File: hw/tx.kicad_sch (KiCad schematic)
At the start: 60 parts, among them Q301 MMBF170, Q302 MMBF170, Q303 MMBF170, Q304 MMBF170, Q305 MMBF170, Q306 MMBF170, Q307 MMBF170, Q308 MMBF170, Q309 MMBF170, Q310 MMBF170, Q311 MMBF170, Q312 MMBF170, T301 BN-43-202_DualPri_CTSec, U301 ICE40UP5K-SG48ITR, U302 CD74ACT541SM96, Y301 40MHz

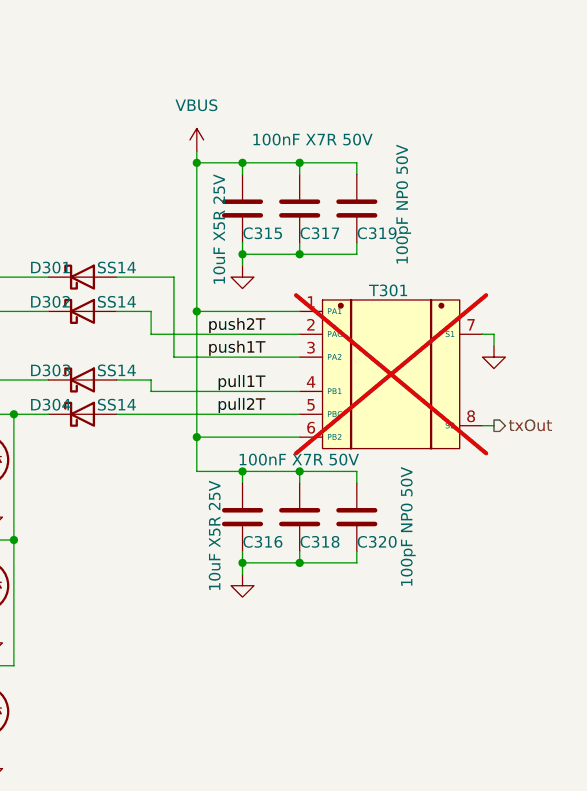
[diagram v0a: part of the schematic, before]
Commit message: Parts ordered for DVT1 build
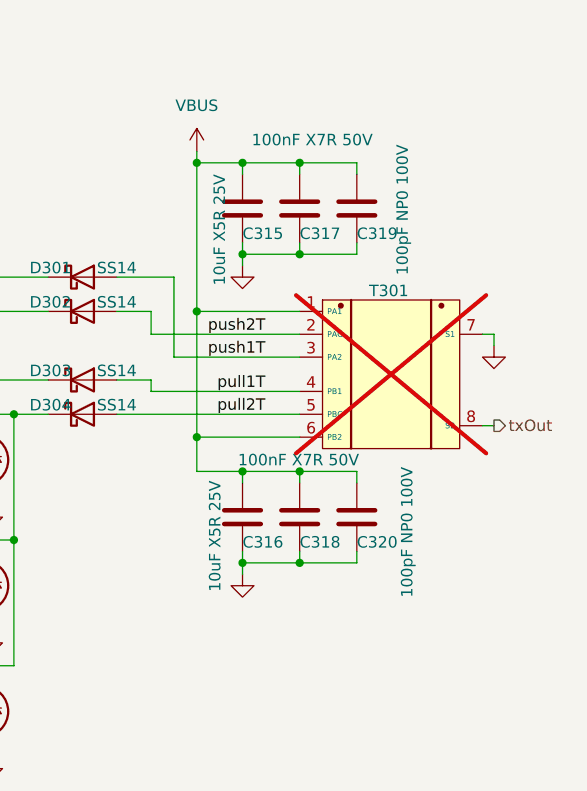
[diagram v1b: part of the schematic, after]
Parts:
- C301, C303, C309, C311, C313, C317, C318, C321: MFG (none) -> Kyocera AVX; MPN (none) -> KGM15BR71H104KT; Mouser_PN (none) -> 581-KGM15BR71H104KT
- C302, C304, C308, C312, C314, C315, C316, C322: MFG (none) -> Kyocera AVX; MPN (none) -> CM105X5R106M25AT; Mouser_PN (none) -> 346-CM105X5R106M25AT
- C305: MFG (none) -> muRata; MPN (none) -> GRM155Z71A105KE1D; Mouser_PN 81-GRM155R61E105KE1D -> 81-GRM155Z71A105KE1D
- C306: MFG (none) -> Kyocera AVX; MPN (none) -> KGM15BR71H104KT; Mouser_PN 80-C0805F104K1RAUTO -> 581-KGM15BR71H104KT
- C307, C310: MFG (none) -> Kyocera AVX; MPN (none) -> CM05X5R475M10AH; Mouser_PN 74-298D475X9010M2T -> 346-CM05X5R475M10AH
- C319, C320: value 100pF NP0 50V -> 100pF NP0 100V; footprint Capacitor_SMD:C_0402_1005Metric -> Capacitor_SMD:C_0603_1608Metric; MFG (none) -> Kyocera AVX; MPN (none) -> KGM15ACG2A101FT; Mouser_PN (none) -> 581-KGM15ACG2A101FT
- D301, D302, D303, D304: MFG (none) -> onsemi; MPN (none) -> SS14; Mouser_PN (none) -> 512-SS14
- Q301, Q302, Q303, Q304, Q305, Q306, Q307, Q308, Q309, Q310, Q311, Q312: MFG (none) -> Diodes inc; MPN (none) -> MMBF170Q-13-F; Mouser_PN (none) -> 621-MMBF170Q-13-F
- R301, R302, R303, R304, R305: MFG (none) -> Vishay; MPN (none) -> MCS04020C1002FE000; Mouser_PN (none) -> 594-MCS04020C1002FE0
- R306, R307, R308, R309, R310, R311, R312, R313, R314, R315, R316, R317, R318: MFG (none) -> Vishay; MPN (none) -> MCT06030C1009FP500; Mouser_PN (none) -> 594-MCT06030C1009FP5
- U301: MFG (none) -> Lattice; MPN (none) -> ICE40UP5K-SG48I; Mouser_PN (none) -> 842-ICE40UP5K-SG48I
- U302: MFG (none) -> TI; MPN (none) -> CD74ACT541SM96; Mouser_PN (none) -> 595-CD74ACT541SM96
- Y301: MFG (none) -> ECS

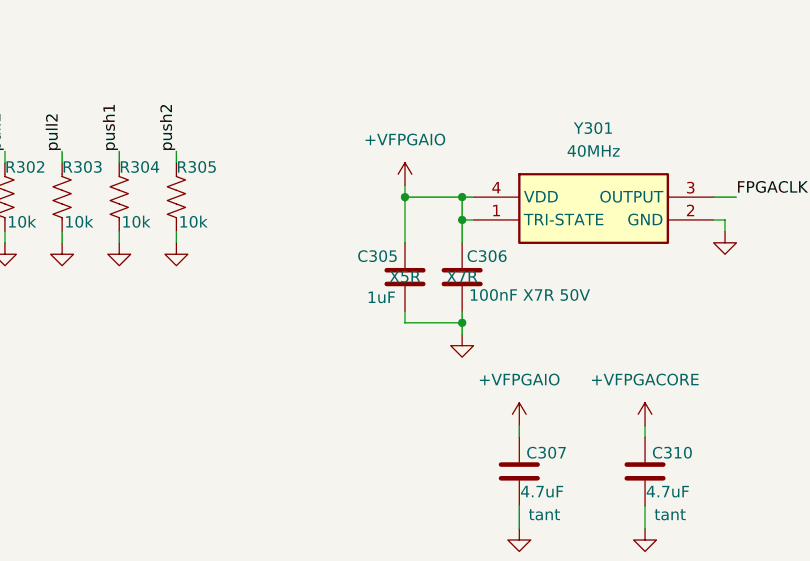
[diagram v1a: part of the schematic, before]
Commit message: About to redo the layout of the tx gate controls to match lengths
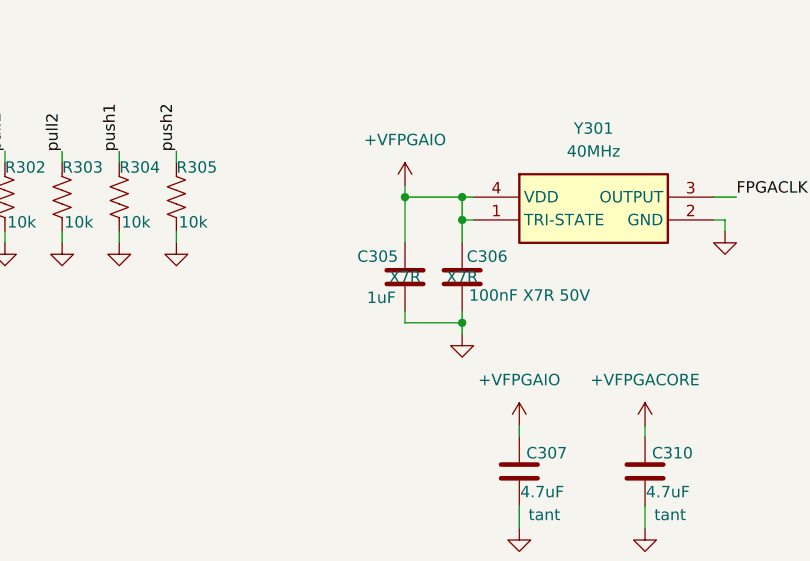
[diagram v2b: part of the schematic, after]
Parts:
- C305: cap-type X5R -> X7R; working-voltage 25V -> 10V
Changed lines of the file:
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@@
 			)
 		)
-		(property "cap-type" "X5R"
+		(property "cap-type" "X7R"
 			(at 69.85 40.64 0)
 			(effects
@@
 			)
 		)
-		(property "working-voltage" "25V"
+		(property "working-voltage" "10V"
 			(at 69.85 40.64 0)
 			(effects

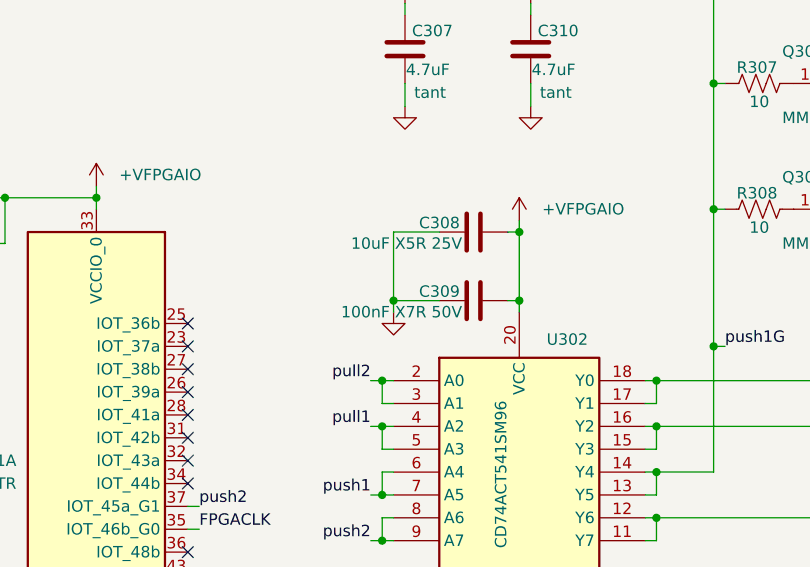
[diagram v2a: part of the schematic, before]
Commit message: Fix huge oopsie with USB diode protection after having fixed the unforgivable polarity reversal and NOT SEEING THIS BUG. I can be an idiot sometimes.
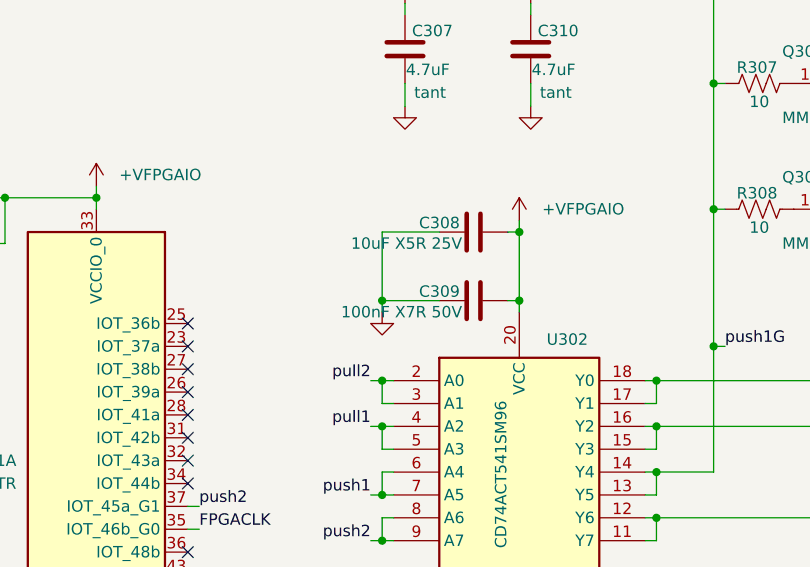
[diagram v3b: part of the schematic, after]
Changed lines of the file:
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@@
 	)
 	(junction
-		(at 81.28 90.17)
-		(diameter 0)
-		(color 0 0 0 0)
-	)
-	(junction
 		(at 76.2 31.75)
 		(diameter 0)
@@
 		(color 0 0 0 0)
 	)
+	(junction
+		(at 80.01 90.17)
+		(diameter 0)
+		(color 0 0 0 0)
+	)
 	(no_connect
 		(at 58.42 175.26)
@@
 	(wire
 		(pts
-			(xy 81.28 91.44) (xy 81.28 90.17)
+			(xy 80.01 91.44) (xy 80.01 90.17)
 		)
 		(stroke
@@
 	(wire
 		(pts
-			(xy 81.28 82.55) (xy 81.28 90.17)
+			(xy 80.01 82.55) (xy 80.01 90.17)
 		)
 		(stroke
@@
 	(wire
 		(pts
+			(xy 80.01 90.17) (xy 86.36 90.17)
+		)
+		(stroke
+			(width 0)
+			(type default)
+		)
+	)
+	(wire
+		(pts
 			(xy 232.41 162.56) (xy 232.41 163.83)
 		)
@@
 	(wire
 		(pts
-			(xy 86.36 82.55) (xy 81.28 82.55)
+			(xy 86.36 82.55) (xy 80.01 82.55)
 		)
 		(stroke
@@
 	(wire
 		(pts
-			(xy 81.28 90.17) (xy 86.36 90.17)
-		)
-		(stroke
-			(width 0)
-			(type default)
-		)
-	)
-	(wire
-		(pts
 			(xy 38.1 83.82) (xy 38.1 78.74)
 		)
@@
 	(symbol
 		(lib_id "power:GND")
-		(at 81.28 91.44 0)
+		(at 80.01 91.44 0)
 		(unit 1)
 		(exclude_from_sim no)
@@
 		(fields_autoplaced yes)
 		(property "Reference" "#PWR0313"
-			(at 81.28 97.79 0)
+			(at 80.01 97.79 0)
 			(effects
 				(font
@@
 		)
 		(property "Value" "GND"
-			(at 81.28 96.52 0)
+			(at 80.01 96.52 0)
 			(effects
 				(font
@@
 		)
 		(property "Footprint" ""
-			(at 81.28 91.44 0)
+			(at 80.01 91.44 0)
 			(effects
 				(font
@@
 		)
 		(property "Datasheet" ""
-			(at 81.28 91.44 0)
+			(at 80.01 91.44 0)
 			(effects
 				(font
@@
 		)
 		(property "Description" "Power symbol creates a global label with name \"GND\" , ground"
-			(at 81.28 91.44 0)
+			(at 80.01 91.44 0)
 			(effects
 				(font

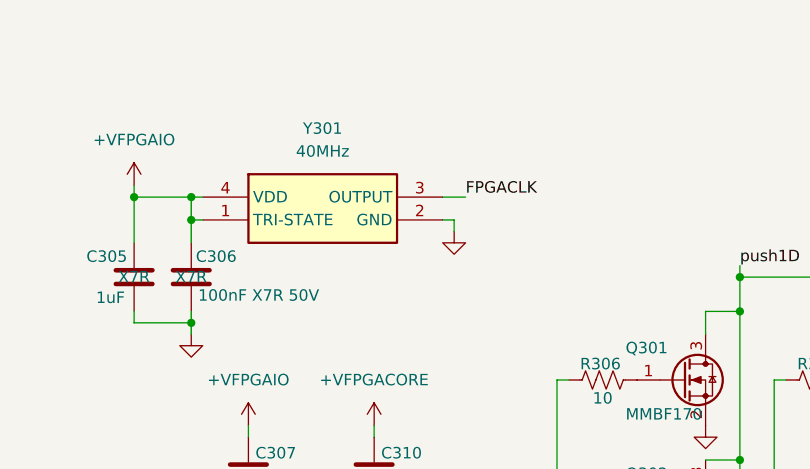
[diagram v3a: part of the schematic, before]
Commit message: Fixed reversed rx/tx on GNSS chip. Solved all ERC and DRC issues
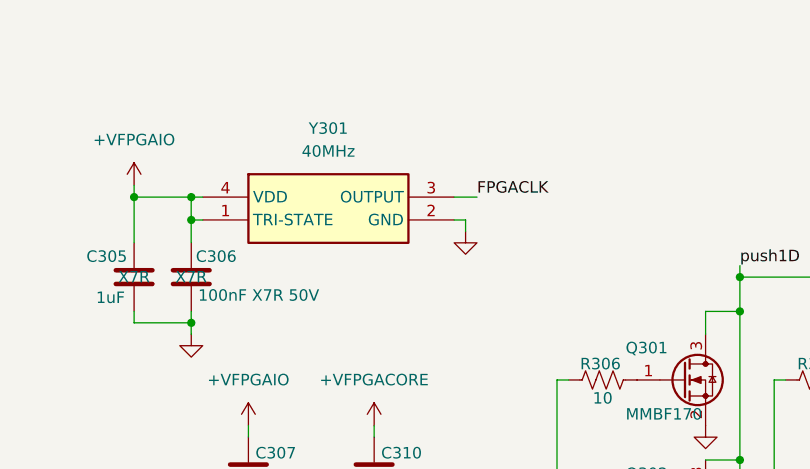
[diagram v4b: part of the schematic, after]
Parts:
- Y301: Manufacturer_Name (none) -> ECS; Manufacturer_Part_Number (none) -> ECS-TXO-2016-33-400-TR; Mouser Part Number (none) -> 520-TXO-2016-33-400T
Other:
- moved on the sheet: Y301
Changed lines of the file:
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@@
 	(wire
 		(pts
-			(xy 104.14 31.75) (xy 106.68 31.75)
+			(xy 105.41 31.75) (xy 107.95 31.75)
 		)
 		(stroke
@@
 	(wire
 		(pts
-			(xy 105.41 34.29) (xy 105.41 35.56)
+			(xy 106.68 34.29) (xy 106.68 35.56)
 		)
 		(stroke
@@
 	(wire
 		(pts
+			(xy 58.42 115.57) (xy 59.69 115.57)
+		)
+		(stroke
+			(width 0)
+			(type default)
+		)
+	)
+	(wire
+		(pts
 			(xy 86.36 82.55) (xy 80.01 82.55)
 		)
@@
 	(wire
 		(pts
-			(xy 58.42 115.57) (xy 59.69 115.57)
-		)
-		(stroke
-			(width 0)
-			(type default)
-		)
-	)
-	(wire
-		(pts
 			(xy 110.49 116.84) (xy 109.22 116.84)
 		)
@@
 	(wire
 		(pts
-			(xy 104.14 34.29) (xy 105.41 34.29)
+			(xy 105.41 34.29) (xy 106.68 34.29)
 		)
 		(stroke
@@
 	)
 	(label "FPGACLK"
-		(at 106.68 31.75 0)
+		(at 107.95 31.75 0)
 		(effects
 			(font
@@
 	(symbol
 		(lib_id "power:GND")
-		(at 105.41 35.56 0)
+		(at 106.68 35.56 0)
 		(unit 1)
 		(exclude_from_sim no)
@@
 		(dnp no)
 		(property "Reference" "#PWR0319"
-			(at 105.41 41.91 0)
+			(at 106.68 41.91 0)
 			(effects
 				(font
@@
 		)
 		(property "Value" "GND"
-			(at 105.156 39.37 0)
+			(at 106.426 39.37 0)
 			(effects
 				(font
@@
 		)
 		(property "Footprint" ""
-			(at 105.41 35.56 0)
+			(at 106.68 35.56 0)
 			(effects
 				(font
@@
 		)
 		(property "Datasheet" ""
-			(at 105.41 35.56 0)
+			(at 106.68 35.56 0)
 			(effects
 				(font
@@
 		)
 		(property "Description" "Power symbol creates a global label with name \"GND\" , ground"
-			(at 105.41 35.56 0)
+			(at 106.68 35.56 0)
 			(effects
 				(font
@@
 		(fields_autoplaced yes)
 		(property "Reference" "Y301"
-			(at 90.805 24.13 0)
+			(at 91.44 24.13 0)
 			(effects
 				(font
@@
 		)
 		(property "Value" "40MHz"
-			(at 90.805 26.67 0)
+			(at 91.44 26.67 0)
 			(effects
 				(font
@@
 				(hide yes)
 			)
+		)
+		(property "Mouser Part Number" "520-TXO-2016-33-400T"
+			(at 111.76 526.67 0)
+			(effects
+				(font
+					(size 1.27 1.27)
+				)
+				(justify left top)
+				(hide yes)
+			)
+		)
+		(property "Manufacturer_Name" "ECS"
+			(at 111.76 726.67 0)
+			(effects
+				(font
+					(size 1.27 1.27)
+				)
+				(justify left top)
+				(hide yes)
+			)
+		)
+		(property "Manufacturer_Part_Number" "ECS-TXO-2016-33-400-TR"
+			(at 111.76 826.67 0)
+			(effects
+				(font
+					(size 1.27 1.27)
+				)
+				(justify left top)
+				(hide yes)
+			)

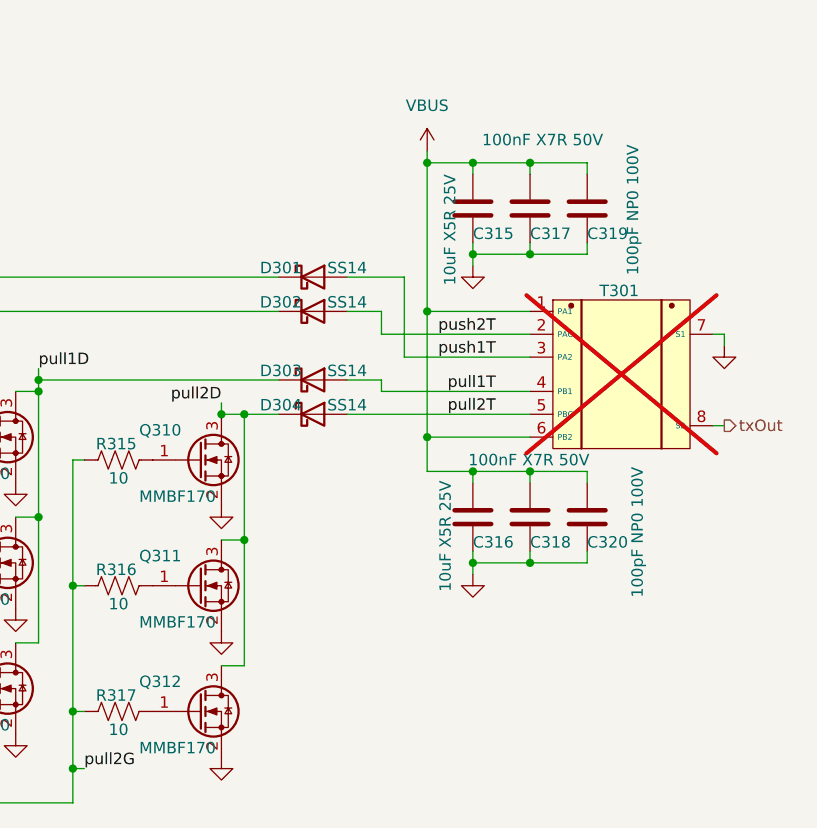
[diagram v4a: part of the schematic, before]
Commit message: Functional but without FPGA loading working well yet
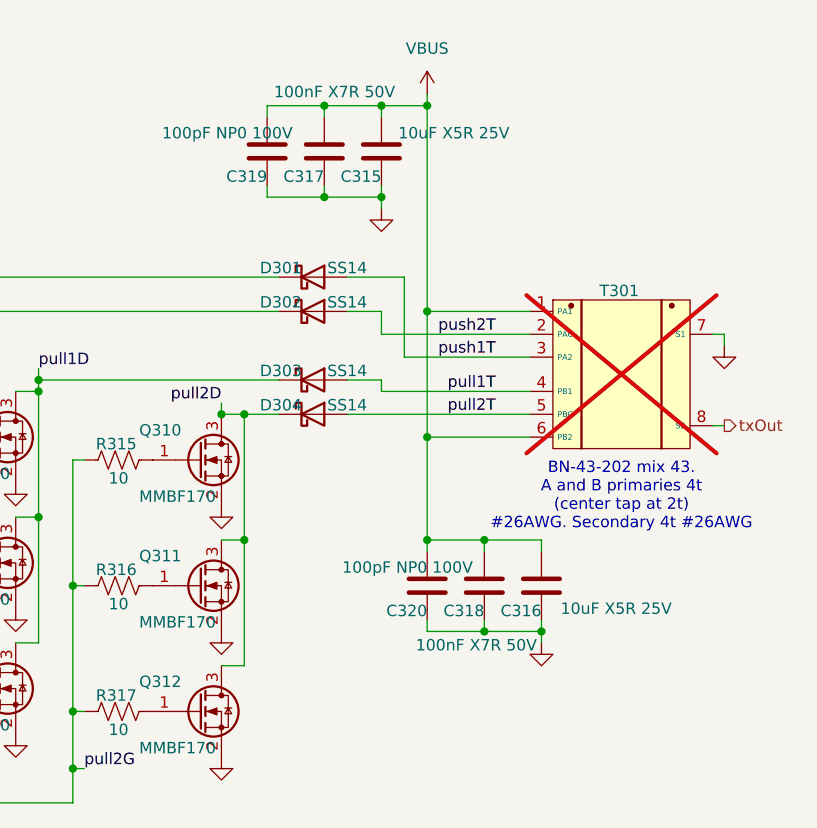
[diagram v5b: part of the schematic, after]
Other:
- note added: "BN-43-202 mix 43. A and B primaries 4t (center tap at 2t) #26AWG. Secondary 4t #26AWG"
- moved on the sheet: C315, C316, C317, C318, C319, C320
